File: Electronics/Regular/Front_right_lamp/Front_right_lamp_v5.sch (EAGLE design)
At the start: 7 parts, among them X2 JST-XH-03-PIN-LONG-PAD

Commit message: BOM on front lamps added
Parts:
- LED1, LED2, LED3: value 2.58 V -> White; CURRENT 0.14 mA -> (none); CURRENT_EMPIRICAL (none) -> 0.14 mA; MANUFACTURER (none) -> LUCKYLIGHT; MANUFACTURER_PART_NUMBER (none) -> LL-504WC2V-W2-3PD; SUPPLIER (none) -> TME; SUPPLIER_PART_NUMBER (none) -> LL-504WC2V-W2-3PD; SUPPLIER_URL (none) -> https://www.tme.eu/pl/details/ll-504wc2v-w2-3pd/diody-led-t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; VOLTAGE_EMPIRICAL (none) -> 2.58 V
- LED4: value 1.88 V -> Yellow; CURRENT 1.42 mA -> (none); CURRENT_EMPIRICAL (none) -> 1.42 mA; MANUFACTURER (none) -> LUCKYLIGHT; MANUFACTURER_PART_NUMBER (none) -> LL-503YD2E-1B; SUPPLIER (none) -> TME; SUPPLIER_PART_NUMBER (none) -> LL-503YD2E-1B; SUPPLIER_URL (none) -> https://www.tme.eu/pl/details/ll-503yd2e-1b/diody-led-tht-o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; VOLTAGE_EMPIRICAL (none) -> 1.88 V
- R1: MANUFACTURER (none) -> ROYAL OHM; MANUFACTURER_PART_NUMBER (none) -> 1206S4J0152T5E; RESISTANCE (none) -> 1.5 kOhm; SUPPLIER (none) -> TME; SUPPLIER_PART_NUMBER (none) -> 1206S4J0152T5E; SUPPLIER_URL (none) -> https://www.tme.eu/pl/details/1206s4j0152t5e/rezystory-smd/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
- R2: MANUFACTURER (none) -> ROYAL OHM; MANUFACTURER_PART_NUMBER (none) -> 1206S4J0681T5E; RESISTANCE (none) -> 680 Ohm; SUPPLIER (none) -> TME; SUPPLIER_PART_NUMBER (none) -> 1206S4J0681T5E; SUPPLIER_URL (none) -> https://www.tme.eu/pl/details/1206s4j0681t5e/rezystory-smd/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
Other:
- note added: "5.1"
- note removed: "5.0"
- moved on the sheet: LED1, LED2, LED3, LED4, R1, R2, X2-1, X2-2, X2-3

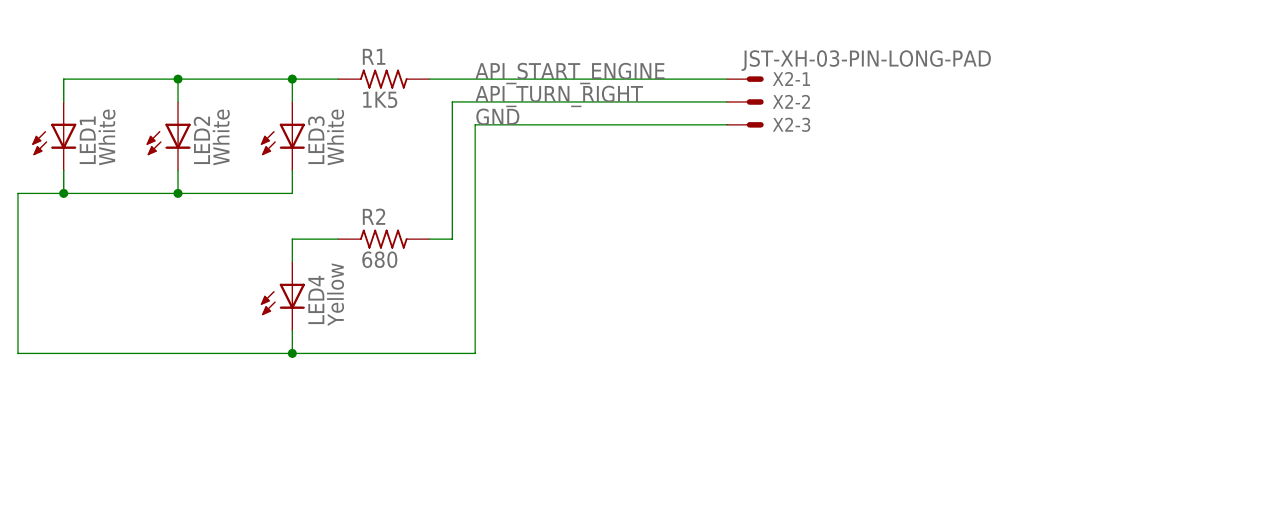
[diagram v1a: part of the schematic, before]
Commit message: BOM on all the lamps added
Note: Version of lamps' projects has increased from x.0 to x.1.

What also has been done:
- some visual refactoring on schematics
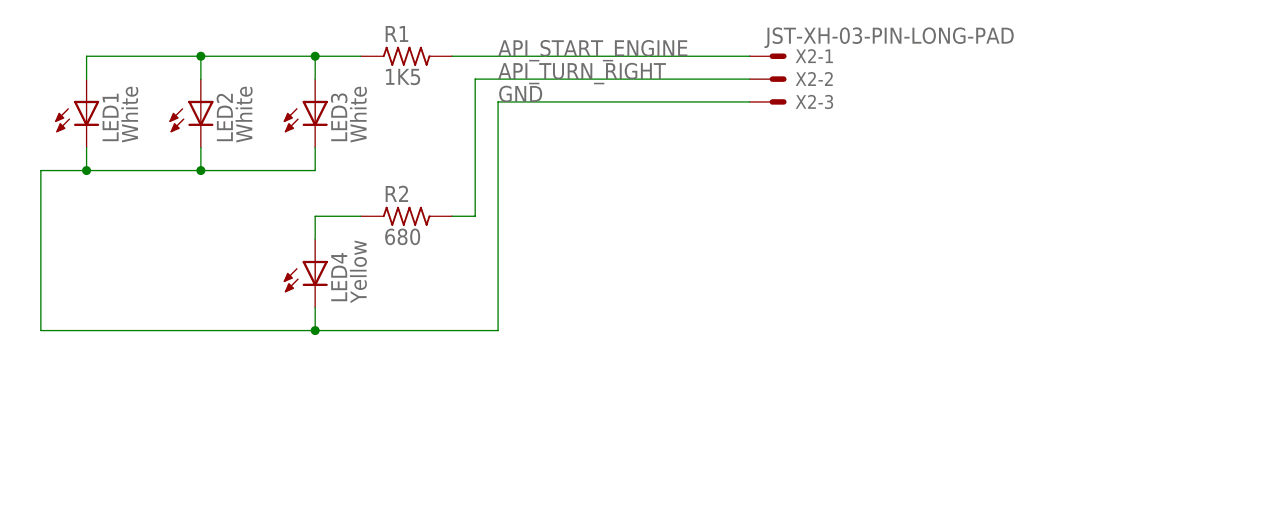
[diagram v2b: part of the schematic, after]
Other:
- moved on the sheet: LED1, LED2, LED3, LED4, R1, R2, X2-1, X2-2, X2-3
